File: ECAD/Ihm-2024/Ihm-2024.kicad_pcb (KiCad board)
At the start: 2 copper layers, 58 x 58 mm, 14 parts, among them SW1 SW_SPDT, SW2 SW_SPDT, SW3 SW_SPDT, SW4 SW_SPDT

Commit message: First routing
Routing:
- net +5V: track 0.00 -> 37.6 mm
- net DAC0: track 0.00 -> 35.7 mm
- net IHM_3: track 0.00 -> 32.1 mm
- net IHM_4: track 0.00 -> 23.8 mm
- net Detection: track 0.00 -> 13.2 mm
- net Couleur: track 0.00 -> 6.09 mm
- net Net-(D4-DOUT): track 0.00 -> 4.58 mm
- net Net-(D3-DOUT): track 0.00 -> 4.58 mm
- net Net-(D2-DOUT): track 0.00 -> 4.58 mm
- net Net-(D1-DOUT): track 0.00 -> 4.58 mm
- net NEO_PIXEL: track 0.00 -> 3.19 mm
- added copper zone on B.Cu, net GND
- added copper zone on F.Cu, net GND
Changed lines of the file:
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@@
   (gr_line (start 171 72) (end 171 120)
     (stroke (width 0.1) (type default)) (layer "Edge.Cuts"))
+  (segment (start 134.64 77) (end 139.535 77) (width 0.5) (layer "F.Cu") (net 1))
+  (segment (start 142.355 74.18) (end 160.33066 74.18) (width 0.5) (layer "F.Cu") (net 1))
+  (segment (start 139.535 77) (end 142.355 74.18) (width 0.5) (layer "F.Cu") (net 1))
+  (segment (start 160.33066 74.18) (end 164.04283 77.89217) (width 0.5) (layer "F.Cu") (net 1))
+  (segment (start 155.575 85.09) (end 156.01 85.525) (width 1) (layer "F.Cu") (net 2))
+  (segment (start 132.01 86.35) (end 132.01 85.16) (width 1) (layer "F.Cu") (net 2))
+  (segment (start 124.01 86.175) (end 125.095 85.09) (width 1) (layer "F.Cu") (net 2))
+  (segment (start 124.01 86.35) (end 124.01 86.175) (width 1) (layer "F.Cu") (net 2))
+  (segment (start 140.01 85.415) (end 140.335 85.09) (width 1) (layer "F.Cu") (net 2))
+  (segment (start 140.335 85.09) (end 147.955 85.09) (width 1) (layer "F.Cu") (net 2))
+  (segment (start 148.01 86.35) (end 148.01 85.145) (width 1) (layer "F.Cu") (net 2))
+  (segment (start 132.08 85.09) (end 140.335 85.09) (width 1) (layer "F.Cu") (net 2))
+  (segment (start 132.01 85.16) (end 132.08 85.09) (width 1) (layer "F.Cu") (net 2))
+  (segment (start 148.01 85.145) (end 147.955 85.09) (width 1) (layer "F.Cu") (net 2))
+  (segment (start 156.01 85.525) (end 156.01 86.35) (width 1) (layer "F.Cu") (net 2))
+  (segment (start 147.955 85.09) (end 155.575 85.09) (width 1) (layer "F.Cu") (net 2))
+  (segment (start 125.095 85.09) (end 132.08 85.09) (width 1) (layer "F.Cu") (net 2))
+  (segment (start 140.01 86.35) (end 140.01 85.415) (width 1) (layer "F.Cu") (net 2))
+  (segment (start 147.79 77) (end 149.86 74.93) (width 0.5) (layer "F.Cu") (net 3))
+  (segment (start 149.86 74.93) (end 160.02 74.93) (width 0.5) (layer "F.Cu") (net 3))
+  (segment (start 160.02 74.93) (end 163.83 78.74) (width 0.5) (layer "F.Cu") (net 3))
+  (segment (start 142.46 77) (end 147.79 77) (width 0.5) (layer "F.Cu") (net 3))
+  (segment (start 160.91 86.35) (end 162.55 86.35) (width 0.5) (layer "F.Cu") (net 4))
+  (segment (start 163.195 86.995) (end 163.195 87.63) (width 0.5) (layer "F.Cu") (net 4))
+  (segment (start 162.55 86.35) (end 163.195 86.995) (width 0.5) (layer "F.Cu") (net 4))
+  (segment (start 155.74 77) (end 157.49 78.75) (width 0.5) (layer "F.Cu") (net 5))
+  (segment (start 150.46 77) (end 155.74 77) (width 0.5) (layer "F.Cu") (net 5))
+  (segment (start 157.49 78.75) (end 161.71868 78.75) (width 0.5) (layer "F.Cu") (net 5))
+  (segment (start 161.71868 78.75) (end 162.56 79.59132) (width 0.5) (layer "F.Cu") (net 5))
+  (segment (start 158.46 77) (end 161.02934 77) (width 0.5) (layer "F.Cu") (net 7))
+  (segment (start 161.02934 77) (end 163.51934 79.49) (width 0.5) (layer "F.Cu") (net 7))
+  (segment (start 133.33 79.5) (end 161.40802 79.5) (width 0.5) (layer "F.Cu") (net 10))
+  (segment (start 130.83 77) (end 133.33 79.5) (width 0.5) (layer "F.Cu") (net 10))
+  (segment (start 161.40802 79.5) (end 161.92151 80.01349) (width 0.5) (layer "F.Cu") (net 10))
+  (segment (start 127.51 77) (end 130.83 77) (width 0.5) (layer "F.Cu") (net 10))
+  (segment (start 152.91 86.55) (end 156.01 89.65) (width 0.5) (layer "F.Cu") (net 15))
+  (segment (start 152.91 86.35) (end 152.91 86.55) (width 0.5) (layer "F.Cu") (net 15))
+  (segment (start 144.91 86.35) (end 144.91 86.55) (width 0.5) (layer "F.Cu") (net 16))
+  (segment (start 144.91 86.55) (end 148.01 89.65) (width 0.5) (layer "F.Cu") (net 16))
+  (segment (start 136.91 86.55) (end 140.01 89.65) (width 0.5) (layer "F.Cu") (net 17))
+  (segment (start 136.91 86.35) (end 136.91 86.55) (width 0.5) (layer "F.Cu") (net 17))
+  (segment (start 128.91 86.55) (end 132.01 89.65) (width 0.5) (layer "F.Cu") (net 18))
+  (segment (start 128.91 86.35) (end 128.91 86.55) (width 0.5) (layer "F.Cu") (net 18))
+  (zone (net 6) (net_name "GND") (layer "F.Cu") (hatch edge 0.5)
+    (priority 1)
+    (connect_pads (clearance 0.5))
+    (min_thickness 0.25) (filled_areas_thickness no)
+    (fill yes (thermal_gap 0.5) (thermal_bridge_width 0.5))
+    (polygon
+      (pts
+        (xy 109.22 63.5)
+        (xy 173.99 63.5)
+        (xy 173.99 128.27)
+        (xy 109.22 128.27)
+      )
+    )
+  )
+  (zone (net 6) (net_name "GND") (layer "B.Cu") (hatch edge 0.5)
+    (connect_pads (clearance 0.5))
+    (min_thickness 0.25) (filled_areas_thickness no)
+    (fill yes (thermal_gap 0.5) (thermal_bridge_width 0.5))
+    (polygon
+      (pts
+        (xy 110.49 64.77)
+        (xy 172.72 64.77)
+        (xy 172.72 127)
+        (xy 110.49 127)
+      )
+    )
+  )
 )

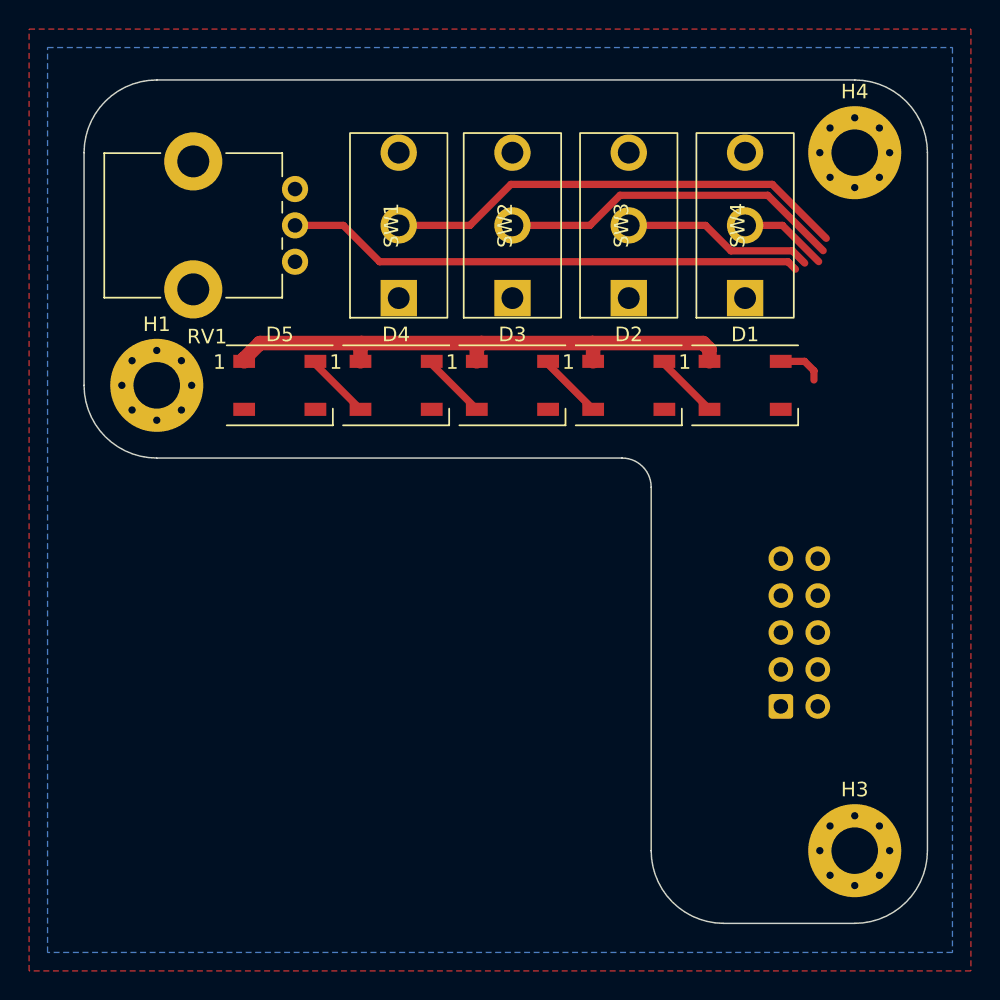
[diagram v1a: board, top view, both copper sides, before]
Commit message: update ICD connector
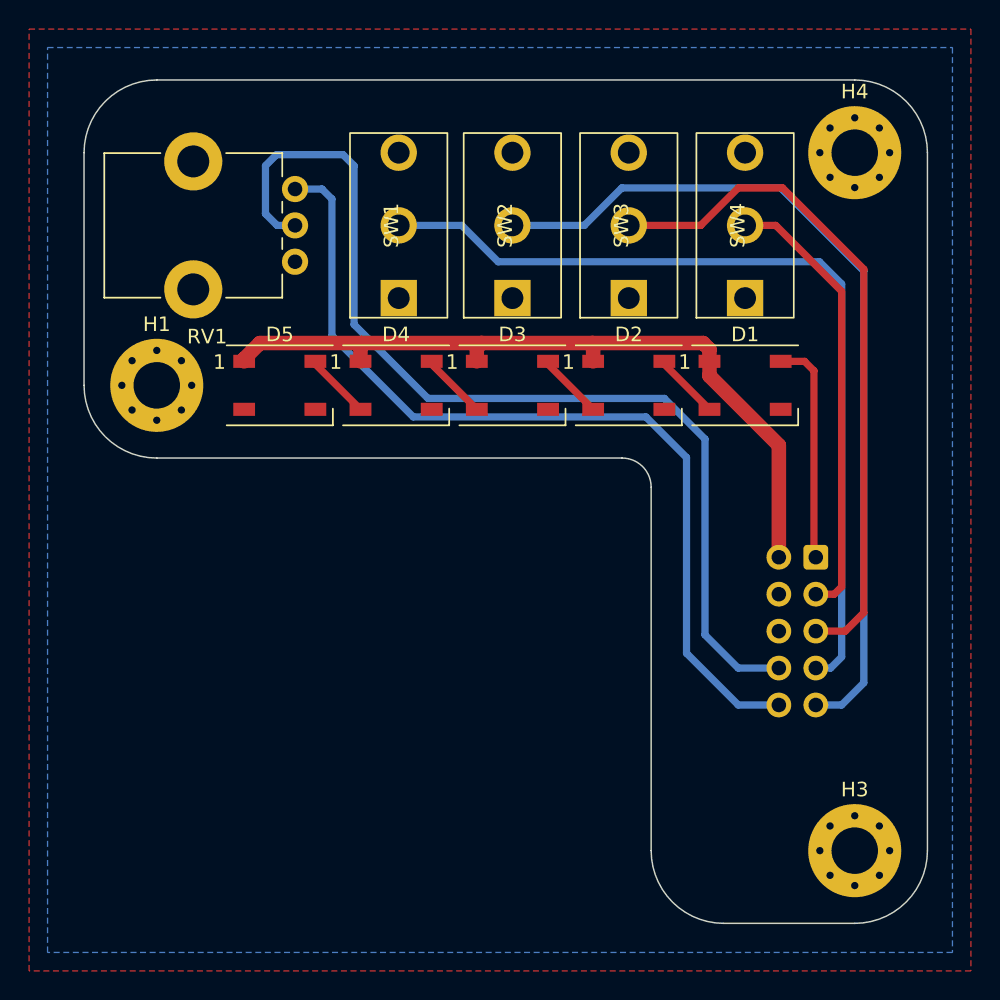
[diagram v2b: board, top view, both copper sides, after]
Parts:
- moved IHM-IO1 10.5 mm to (163.3, 99.8), turned to 180 degrees
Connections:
- IHM-IO1 pad 1: IHM_3 -> NEO_PIXEL
- IHM-IO1 pad 10: DAC0 -> +3V3
- IHM-IO1 pad 3: IHM_4 -> Couleur
- IHM-IO1 pad 4: NEO_PIXEL -> DAC1
- IHM-IO1 pad 7: Couleur -> IHM_3
- IHM-IO1 pad 8: DAC1 -> DAC0
- IHM-IO1 pad 9: +3V3 -> IHM_4
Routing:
- net +3V3: track 0.00 -> 61.4 mm
- net IHM_4: track 23.8 -> 59.9 mm
- net DAC0: track 35.7 -> 70.2 mm
- net Detection: track 13.2 -> 47.0 mm
- net IHM_3: track 32.1 -> 59.9 mm
- net Couleur: track 6.09 -> 30.8 mm
- net +5V: track 37.6 -> 53.0 mm
- net NEO_PIXEL: track 3.19 -> 15.4 mm

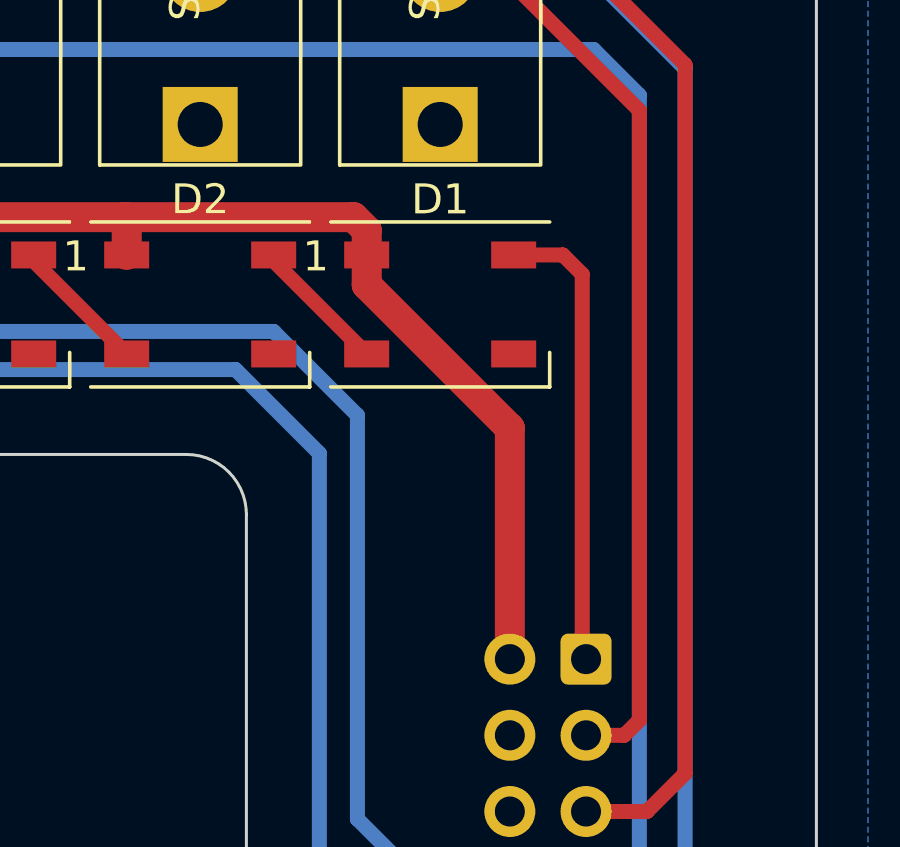
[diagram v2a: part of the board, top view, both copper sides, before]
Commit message: add capacitor
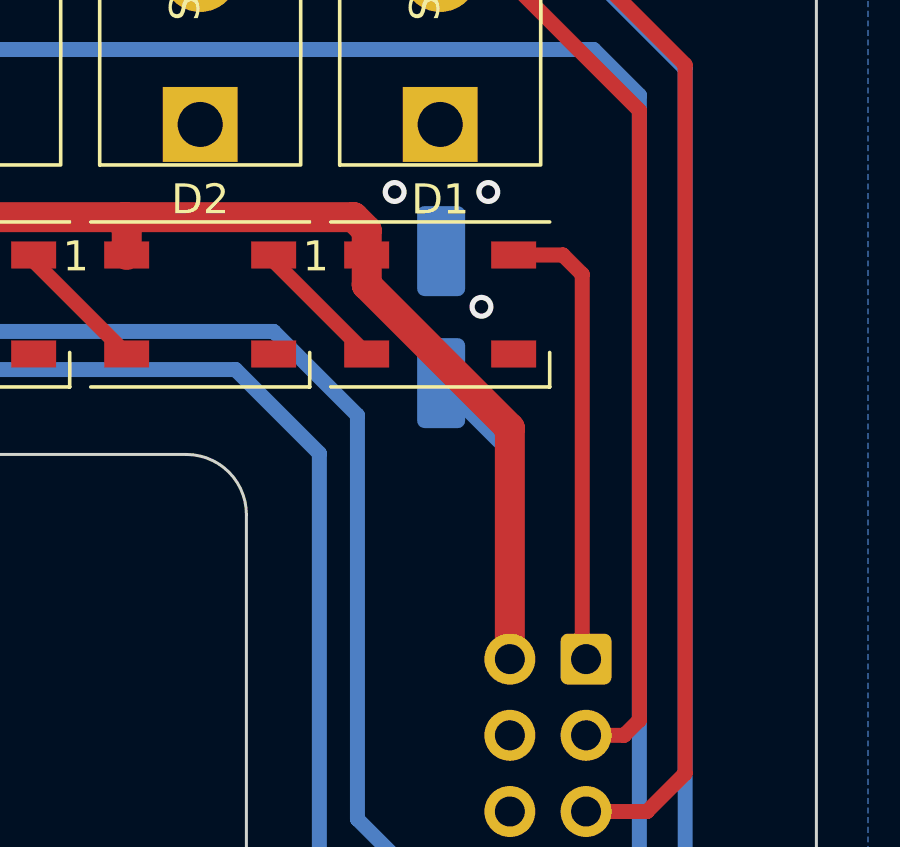
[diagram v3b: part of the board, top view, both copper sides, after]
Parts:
- added C1: 22uF, Capacitor_SMD:CP_Elec_5x5.4, B.Cu at (158.5, 88.4)
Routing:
- net +5V: track 53.0 -> 63.2 mm
- net GND: vias 0 -> 3
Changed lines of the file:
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@@
+    )
+  )
+  (footprint "Capacitor_SMD:CP_Elec_5x5.4" (layer "B.Cu")
+    (at 158.491582 88.422253 90)
+    (descr "SMD capacitor, aluminum electrolytic, Nichicon, 5.0x5.4mm")
+    (tags "capacitor electrolytic")
+    (property "Sheetfile" "Ihm-2024.kicad_sch")
+    (property "Sheetname" "")
+    (property "ki_description" "Polarized capacitor, small symbol")
+    (property "ki_keywords" "cap capacitor")
+    (attr smd)
+    (fp_text reference "C1" (at 0 3.7 90) (layer "B.SilkS")
+        (effects (font (size 1 1) (thickness 0.15)) (justify mirror))
+    )
+    (fp_text value "22uF" (at 0 -3.7 90) (layer "B.Fab")
+        (effects (font (size 1 1) (thickness 0.15)) (justify mirror))
+    )
+    (fp_text user "${REFERENCE}" (at 0 0 90) (layer "B.Fab")
+        (effects (font (size 1 1) (thickness 0.15)) (justify mirror))
+    )
+    (fp_line (start -3.625 1.685) (end -3 1.685)
+      (stroke (width 0.12) (type solid)) (layer "B.SilkS"))
+    (fp_line (start -3.3125 1.9975) (end -3.3125 1.3725)
+      (stroke (width 0.12) (type solid)) (layer "B.SilkS"))
+    (fp_line (start -2.76 -1.695563) (end -2.76 -1.06)
+      (stroke (width 0.12) (type solid)) (layer "B.SilkS"))
+    (fp_line (start -2.76 -1.695563) (end -1.695563 -2.76)
+      (stroke (width 0.12) (type solid)) (layer "B.SilkS"))
+    (fp_line (start -2.76 1.695563) (end -2.76 1.06)
+      (stroke (width 0.12) (type solid)) (layer "B.SilkS"))
+    (fp_line (start -2.76 1.695563) (end -1.695563 2.76)
+      (stroke (width 0.12) (type solid)) (layer "B.SilkS"))
+    (fp_line (start -1.695563 -2.76) (end 2.76 -2.76)
+      (stroke (width 0.12) (type solid)) (layer "B.SilkS"))
+    (fp_line (start -1.695563 2.76) (end 2.76 2.76)
+      (stroke (width 0.12) (type solid)) (layer "B.SilkS"))
+    (fp_line (start 2.76 -2.76) (end 2.76 -1.06)
+      (stroke (width 0.12) (type solid)) (layer "B.SilkS"))
+    (fp_line (start 2.76 2.76) (end 2.76 1.06)
+      (stroke (width 0.12) (type solid)) (layer "B.SilkS"))
+    (fp_line (start -3.95 -1.05) (end -2.9 -1.05)
+      (stroke (width 0.05) (type solid)) (layer "B.CrtYd"))
+    (fp_line (start -3.95 1.05) (end -3.95 -1.05)
+      (stroke (width 0.05) (type solid)) (layer "B.CrtYd"))
+    (fp_line (start -2.9 -1.75) (end -1.75 -2.9)
+      (stroke (width 0.05) (type solid)) (layer "B.CrtYd"))
+    (fp_line (start -2.9 -1.05) (end -2.9 -1.75)
+      (stroke (width 0.05) (type solid)) (layer "B.CrtYd"))
+    (fp_line (start -2.9 1.05) (end -3.95 1.05)
+      (stroke (width 0.05) (type solid)) (layer "B.CrtYd"))
+    (fp_line (start -2.9 1.75) (end -2.9 1.05)
+      (stroke (width 0.05) (type solid)) (layer "B.CrtYd"))
+    (fp_line (start -2.9 1.75) (end -1.75 2.9)
+      (stroke (width 0.05) (type solid)) (layer "B.CrtYd"))
+    (fp_line (start -1.75 -2.9) (end 2.9 -2.9)
+      (stroke (width 0.05) (type solid)) (layer "B.CrtYd"))
+    (fp_line (start -1.75 2.9) (end 2.9 2.9)
+      (stroke (width 0.05) (type solid)) (layer "B.CrtYd"))
+    (fp_line (start 2.9 -1.05) (end 2.9 -2.9)
+      (stroke (width 0.05) (type solid)) (layer "B.CrtYd"))
+    (fp_line (start 2.9 1.05) (end 3.95 1.05)
+      (stroke (width 0.05) (type solid)) (layer "B.CrtYd"))
+    (fp_line (start 2.9 2.9) (end 2.9 1.05)
+      (stroke (width 0.05) (type solid)) (layer "B.CrtYd"))
+    (fp_line (start 3.95 -1.05) (end 2.9 -1.05)
+      (stroke (width 0.05) (type solid)) (layer "B.CrtYd"))
+    (fp_line (start 3.95 1.05) (end 3.95 -1.05)
+      (stroke (width 0.05) (type solid)) (layer "B.CrtYd"))
+    (fp_line (start -2.65 -1.65) (end -1.65 -2.65)
+      (stroke (width 0.1) (type solid)) (layer "B.Fab"))
+    (fp_line (start -2.65 1.65) (end -2.65 -1.65)
+      (stroke (width 0.1) (type solid)) (layer "B.Fab"))
+    (fp_line (start -2.65 1.65) (end -1.65 2.65)
+      (stroke (width 0.1) (type solid)) (layer "B.Fab"))
+    (fp_line (start -2.033956 1.2) (end -1.533956 1.2)
+      (stroke (width 0.1) (type solid)) (layer "B.Fab"))
+    (fp_line (start -1.783956 1.45) (end -1.783956 0.95)
+      (stroke (width 0.1) (type solid)) (layer "B.Fab"))
+    (fp_line (start -1.65 -2.65) (end 2.65 -2.65)
+      (stroke (width 0.1) (type solid)) (layer "B.Fab"))
+    (fp_line (start -1.65 2.65) (end 2.65 2.65)
+      (stroke (width 0.1) (type solid)) (layer "B.Fab"))
+    (fp_line (start 2.65 2.65) (end 2.65 -2.65)
+      (stroke (width 0.1) (type solid)) (layer "B.Fab"))
+    (fp_circle (center 0 0) (end 2.5 0)
+      (stroke (width 0.1) (type solid)) (fill none) (layer "B.Fab"))
+    (pad "1" smd roundrect (at -2.2 0 90) (size 3 1.6) (layers "B.Cu" "B.Paste" "B.Mask") (roundrect_rratio 0.15625)
+      (net 2 "+5V") (pintype "passive"))
+    (pad "2" smd roundrect (at 2.2 0 90) (size 3 1.6) (layers "B.Cu" "B.Paste" "B.Mask") (roundrect_rratio 0.15625)
+      (net 6 "GND") (pintype "passive"))
+    (model "${KICAD6_3DMODEL_DIR}/Capacitor_SMD.3dshapes/CP_Elec_5x5.4.wrl"
+      (offset (xyz 0 0 0))
+      (scale (xyz 1 1 1))
+      (rotate (xyz 0 0 0))
     )
   )
@@
   (segment (start 156.01 87.348) (end 160.782 92.12) (width 1) (layer "F.Cu") (net 2))
   (segment (start 156.01 86.35) (end 156.01 87.348) (width 1) (layer "F.Cu") (net 2))
+  (segment (start 160.782 92.912671) (end 160.782 99.822) (width 0.5) (layer "B.Cu") (net 2))
+  (segment (start 158.491582 90.622253) (end 160.782 92.912671) (width 0.5) (layer "B.Cu") (net 2))
   (segment (start 149.987 74.422) (end 160.909 74.422) (width 0.5) (layer "B.Cu") (net 3))
   (segment (start 160.909 74.422) (end 166.624 80.137) (width 0.5) (layer "B.Cu") (net 3))
@@
   (segment (start 161.036 74.422) (end 166.624 80.01) (width 0.5) (layer "F.Cu") (net 5))
   (segment (start 166.624 103.632) (end 165.354 104.902) (width 0.5) (layer "F.Cu") (net 5))
+  (via (at 156.941954 84.251532) (size 0.8) (drill 0.45) (layers "F.Cu" "B.Cu") (free) (net 6))
+  (via (at 159.83586 88.078013) (size 0.8) (drill 0.45) (layers "F.Cu" "B.Cu") (free) (net 6))
+  (via (at 160.063531 84.251532) (size 0.8) (drill 0.45) (layers "F.Cu" "B.Cu") (free) (net 6))
   (segment (start 160.566 77) (end 165.1 81.534) (width 0.5) (layer "F.Cu") (net 7))
   (segment (start 158.46 77) (end 160.566 77) (width 0.5) (layer "F.Cu") (net 7))

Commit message: update silkscreen
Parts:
- added G***: LOGO, LOGO, F.Cu at (159.0, 105.0)
- added G***: LOGO, LOGO, F.Cu at (167.8, 112.6)
- added kibuzzard-64A1DF46: G***, kibuzzard-64A1DF46, F.Cu at (157.5, 99.8)
- added kibuzzard-64A1DF73: G***, kibuzzard-64A1DF73, F.Cu at (157.2, 110.0)
- added kibuzzard-64A1DFA1: G***, kibuzzard-64A1DFA1, F.Cu at (158.5, 69.6)
- added kibuzzard-64A1DFBF: G***, kibuzzard-64A1DFBF, F.Cu at (150.6, 69.6)
- added kibuzzard-64A1DFD1: G***, kibuzzard-64A1DFD1, F.Cu at (142.5, 69.6)
- added kibuzzard-64A1DFD6: G***, kibuzzard-64A1DFD6, F.Cu at (134.6, 69.6)
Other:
- board text added: "Barbatronic"
- board text added: "Karibous 2023-24"
